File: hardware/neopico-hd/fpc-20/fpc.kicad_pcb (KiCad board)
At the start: 2 copper layers, 46.9 x 36.2 mm, 3 parts, among them J1 Conn_02x27_Pin, J2 Conn_01x20_Pin

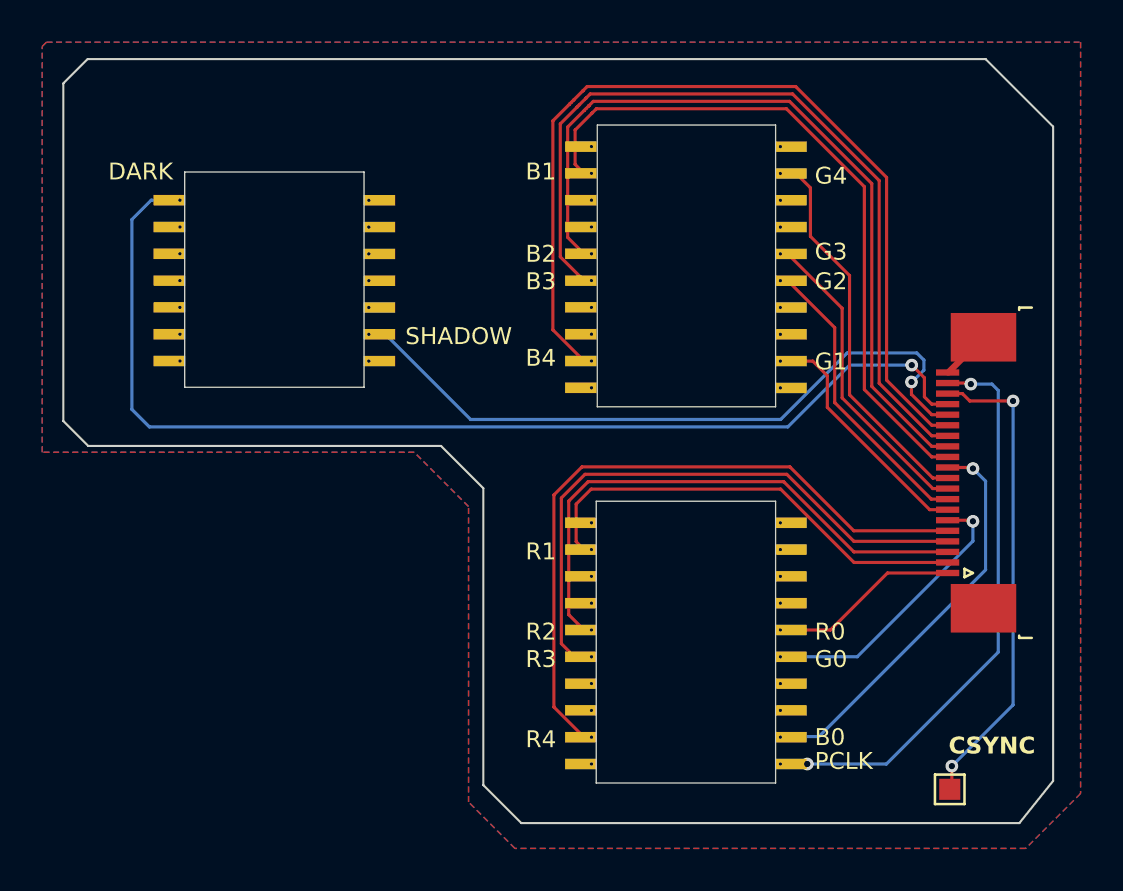
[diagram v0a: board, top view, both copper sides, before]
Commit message: Update FPC 20
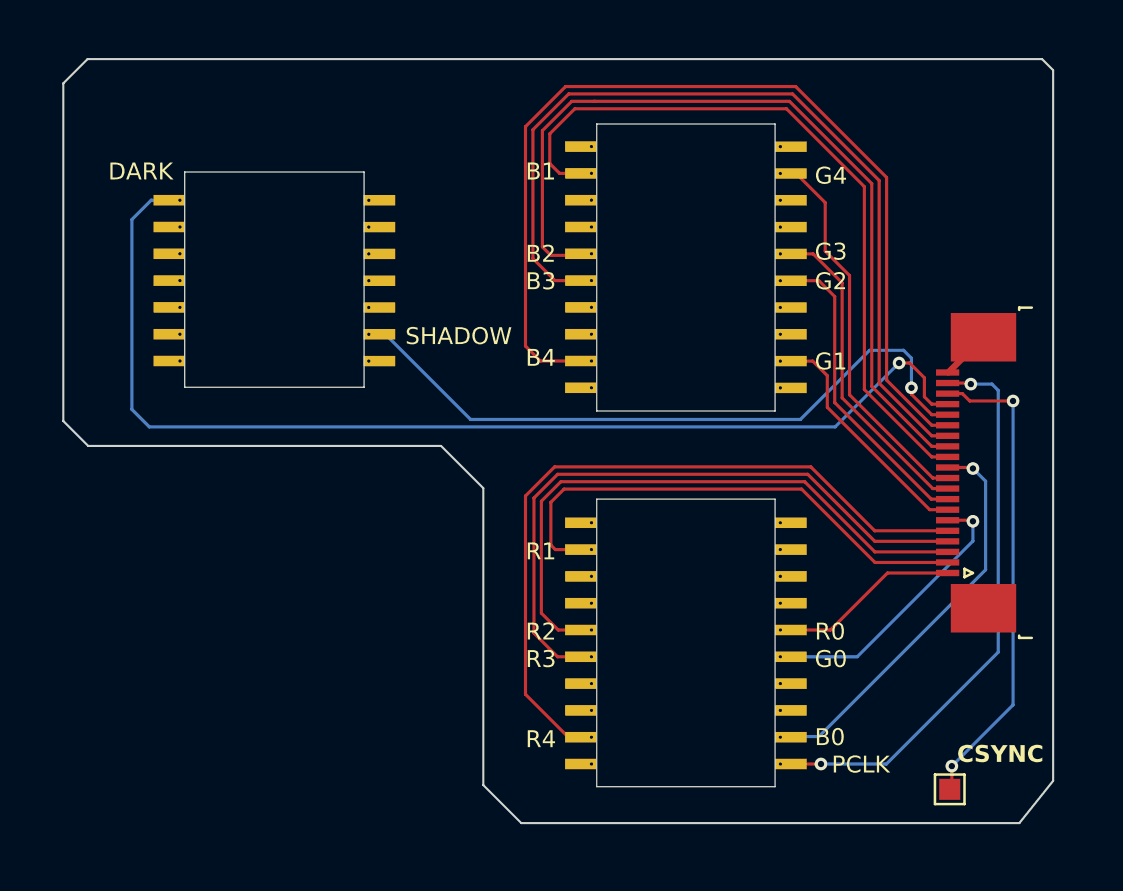
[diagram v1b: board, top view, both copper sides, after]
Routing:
- net B4: track 43.6 -> 46.5 mm
- net B2: track 37.2 -> 40.0 mm
- net R1: track 21.6 -> 24.2 mm
- net R2: track 26.1 -> 28.7 mm
- net B3: track 39.2 -> 41.7 mm
- net B1: track 32.8 -> 35.1 mm
- net R4: track 32.5 -> 34.8 mm
- net R3: track 28.3 -> 30.6 mm
- net G2: track 13.9 -> 14.8 mm
- net G3: track 14.7 -> 15.4 mm
- net SHADOW: track 33.4 -> 32.7 mm
- removed copper zone on B.Cu, net GND
- removed copper zone on F.Cu, net GND
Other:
- outline, holes or cut-outs redrawn
- board text added: "R1"
- board text added: "Stiffener - Polyimide 0.2mm"

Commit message: Add GND plane
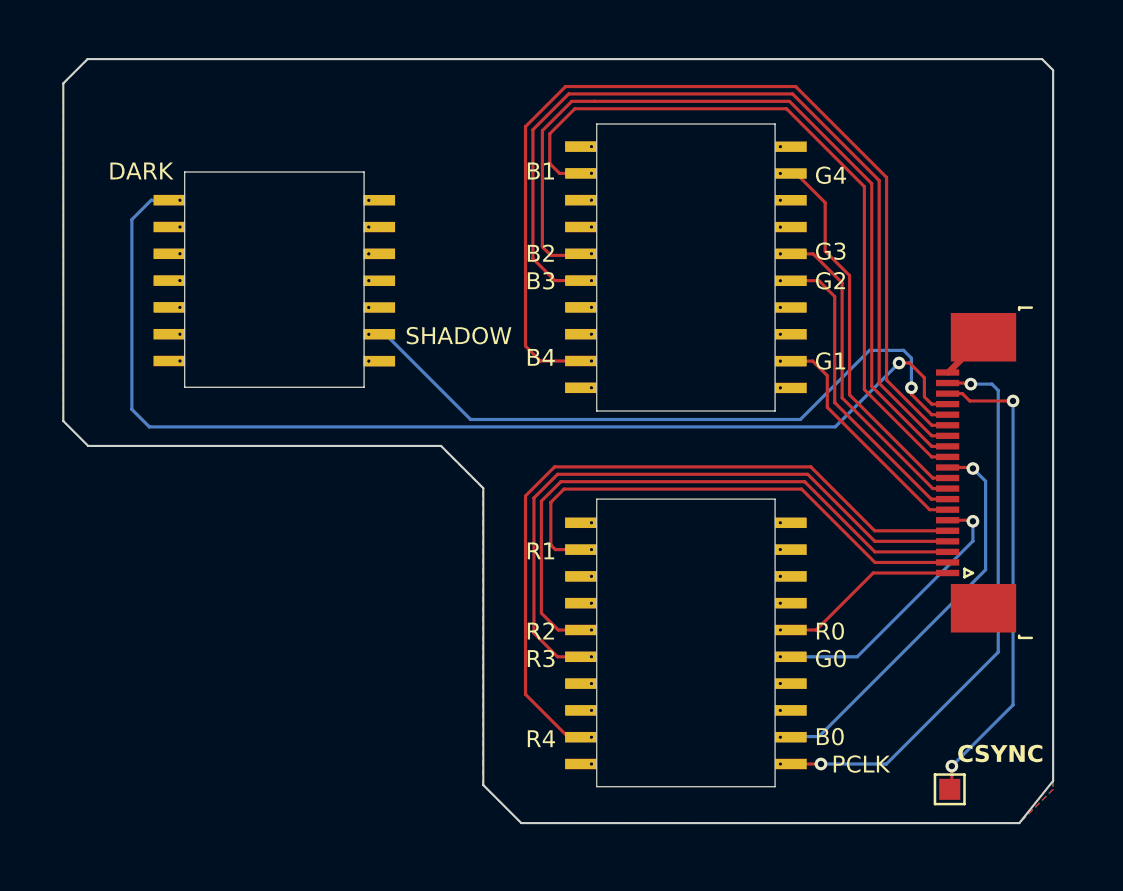
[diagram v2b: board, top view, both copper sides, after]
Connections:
- J1 pad 10: unconnected-(J1-Pin_10-Pad10) -> GND
- J1 pad 30: unconnected-(J1-Pin_30-Pad30) -> GND
- J1 pad 47: unconnected-(J1-Pin_47-Pad47) -> GND
- J2 pad MP: GND -> (no net)
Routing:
- added copper zone on B.Cu, net GND
- added copper zone on F.Cu, net GND
